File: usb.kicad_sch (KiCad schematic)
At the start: 27 parts, among them J2 USB4105, J3 USB-A-S-F-B-VU, U1 MX6UL-VM, U11 TPD4EUSB30, U12 74LVC1G04, U13 D5V0H1B2LP, U4 TUSB320, U5 AP22814AW5, U6 TPD4EUSB30, U7 D5V0H1B2LP

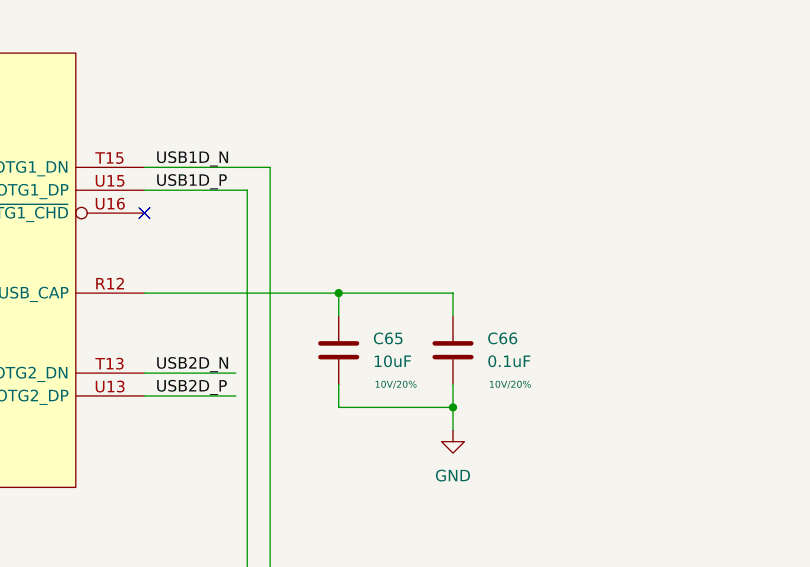
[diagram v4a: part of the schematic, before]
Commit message: lots of routing, ddr length matching done
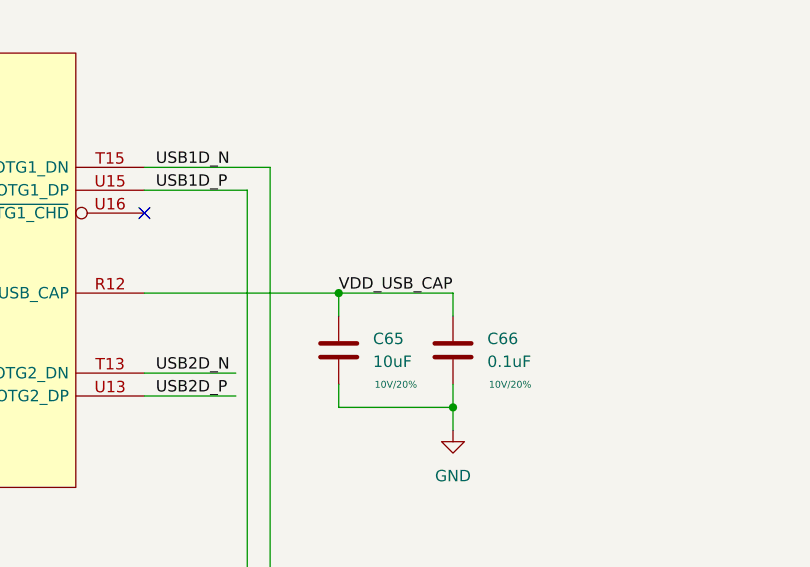
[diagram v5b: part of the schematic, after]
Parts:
- J3: footprint imx6ull-sbc:SAMTEC_USB-A-S-X-X-VU -> qsbc-zero:SAMTEC_USB-A-S-X-X-VU
- U1: footprint imx6ull-sbc:SOT1534-2 -> qsbc-zero:SOT1534-2; symbol imx6ull-sbc:MX6UL-VM -> qsbc-zero:MX6UL-VM
- U11, U6: symbol imx6ull-sbc:TPD4EUSB30 -> qsbc-zero:TPD4EUSB30
- U13, U7: footprint imx6ull-sbc:DFN100X60X45-2N -> qsbc-zero:DFN100X60X45-2N; symbol imx6ull-sbc:D5V0H1B2LP -> qsbc-zero:D5V0H1B2LP
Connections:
- net VDD_USB_CAP: now reaches C65.1, C66.1, U1.R12 (VDD_USB_CAP)
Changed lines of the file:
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@@
     (stroke (width 0) (type default) (color 0 0 0 0))
+  )
+  (label "VDD_USB_CAP" (at 130.81 80.01 0)
+    (effects (font (size 1.27 1.27)) (justify left bottom))
   )
   (label "~{USB1_INT}" (at 35.56 22.86 0)
@@
     (pin "1")
   )
-  (symbol (lib_id "imx6ull-sbc:D5V0H1B2LP") (at 298.45 60.96 270) (unit 1)
+  (symbol (lib_id "qsbc-zero:D5V0H1B2LP") (at 298.45 60.96 270) (unit 1)
     (in_bom yes) (on_board yes) (fields_autoplaced)
     (property "Reference" "U13" (id 0) (at 299.72 59.6899 90)
@@
       (effects (font (size 1.27 1.27)) (justify left))
     )
-    (property "Footprint" "imx6ull-sbc:DFN100X60X45-2N" (id 2) (at 299.72 61.087 0)
+    (property "Footprint" "qsbc-zero:DFN100X60X45-2N" (id 2) (at 299.72 61.087 0)
       (effects (font (size 1.27 1.27)) hide)
     )
@@
     (pin "1")
   )
-  (symbol (lib_id "imx6ull-sbc:MX6UL-VM") (at 76.2 53.34 0) (unit 8)
+  (symbol (lib_id "qsbc-zero:MX6UL-VM") (at 76.2 53.34 0) (unit 8)
     (in_bom yes) (on_board yes) (fields_autoplaced)
     (property "Reference" "U1" (id 0) (at 76.2 46.99 0)
@@
       (effects (font (size 1.524 1.524)))
     )
-    (property "Footprint" "imx6ull-sbc:SOT1534-2" (id 2) (at 89.154 82.804 0)
+    (property "Footprint" "qsbc-zero:SOT1534-2" (id 2) (at 89.154 82.804 0)
       (effects (font (size 1.524 1.524)) hide)
     )
@@
     (pin "1")
   )
-  (symbol (lib_id "imx6ull-sbc:TPD4EUSB30") (at 241.3 86.36 0) (unit 1)
+  (symbol (lib_id "qsbc-zero:TPD4EUSB30") (at 241.3 86.36 0) (unit 1)
     (in_bom yes) (on_board yes) (fields_autoplaced)
     (property "Reference" "U11" (id 0) (at 241.3 73.1314 0))
@@
     (pin "1")
   )
-  (symbol (lib_id "imx6ull-sbc:TPD4EUSB30") (at 135.89 207.01 0) (unit 1)
+  (symbol (lib_id "qsbc-zero:TPD4EUSB30") (at 135.89 207.01 0) (unit 1)
     (in_bom yes) (on_board yes) (fields_autoplaced)
     (property "Reference" "U6" (id 0) (at 135.89 193.7814 0))
@@
     (pin "2")
   )
-  (symbol (lib_id "imx6ull-sbc:D5V0H1B2LP") (at 181.61 208.28 0) (unit 1)
+  (symbol (lib_id "qsbc-zero:D5V0H1B2LP") (at 181.61 208.28 0) (unit 1)
     (in_bom yes) (on_board yes) (fields_autoplaced)
     (property "Reference" "U7" (id 0) (at 181.61 203.2 0))
     (property "Value" "D5V0H1B2LP" (id 1) (at 181.61 205.74 0))
-    (property "Footprint" "imx6ull-sbc:DFN100X60X45-2N" (id 2) (at 181.737 207.01 0)
+    (property "Footprint" "qsbc-zero:DFN100X60X45-2N" (id 2) (at 181.737 207.01 0)
       (effects (font (size 1.27 1.27)) hide)
     )
@@
     (property "Reference" "J3" (id 0) (at 222.25 40.64 0))
     (property "Value" "USB-A-S-F-B-VU" (id 1) (at 222.25 43.18 0))
-    (property "Footprint" "imx6ull-sbc:SAMTEC_USB-A-S-X-X-VU" (id 2) (at 226.06 54.61 0)
-      (effects (font (size 1.27 1.27)) hide)
-    )
+    (property "Footprint" "qsbc-zero:SAMTEC_USB-A-S-X-X-VU" (id 2) (at 226.06 54.61 0)
+      (effects (font (size 1.27 1.27)) hide)
+    )

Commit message: more pcb work, bom work
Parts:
- C63, C64, C69: DigiKey_PN (none) -> 490-13409-1-ND; MPN (none) -> GCM155C71A105KE38D
- C65: DigiKey_PN (none) -> 1276-1450-1-ND; MPN (none) -> CL05A106MP5NUNC
- C66: footprint Capacitor_SMD:C_0201_0603Metric -> Capacitor_SMD:C_0402_1005Metric; DigiKey_PN (none) -> 490-14603-1-ND; MPN (none) -> GRM155R71E104KE14J; Rating 10V/20% -> 25V/20%
- C67, C94: DigiKey_PN (none) -> 490-14603-1-ND; MPN (none) -> GRM155R71E104KE14J; Rating 10V/20% -> 25V/20%
- C68, C95: DigiKey_PN (none) -> 490-14603-1-ND; MPN (none) -> GRM155R71E104KE14J; Rating 6.3V/20% -> 25V/20%
- C82, C93: DigiKey_PN (none) -> 478-8198-1-ND; MPN (none) -> F931A107MBA
- J2: DigiKey_PN (none) -> 2073-USB4105-GF-ACT-ND; MPN (none) -> USB4105-GF-A
- J3: DigiKey_PN (none) -> SAM10862-ND; MPN (none) -> USB-A-S-F-B-VU
- R10, R11, R38, R39: DigiKey_PN (none) -> 311-10KJRCT-ND; MPN (none) -> RC0402JR-0710KL
- R40: DNP DNP -> (none); DigiKey_PN (none) -> 311-0.0LRCT-ND; MPN (none) -> RC0402FR-070RL
- R9: footprint Capacitor_SMD:C_0402_1005Metric -> Resistor_SMD:R_0402_1005Metric; DigiKey_PN (none) -> 311-1.0MJRCT-ND; MPN (none) -> RC0402JR-071ML
- U1: DigiKey_PN (none) -> 568-14995-ND; MPN (none) -> MCIMX6Y2DVM09AB
- U11, U6: DigiKey_PN (none) -> 296-28063-1-ND; MPN (none) -> TPD4EUSB30DQAR
- U12: DNP (none) -> DNP; DigiKey_PN (none) -> 296-26588-1-ND; MPN (none) -> SN74LVC1G04QDBVRQ1
- U13, U7: DigiKey_PN (none) -> D5V0H1B2LP-7BDICT-ND; MPN (none) -> D5V0H1B2LP-7B
- U4: DigiKey_PN (none) -> 296-43142-1-ND; MPN (none) -> TUSB320LAIRWBR
- U5: value AP22814AW5 -> AP22811B; DigiKey_PN (none) -> AP22811BW5-7DICT-ND; MPN (none) -> AP22811BW5-7
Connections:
- net USB_VBUS: now also C82.1
- net VBUS_1: no longer C82.1
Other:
- moved on the sheet: C82

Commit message: add basic readme, rev 1 of pcb
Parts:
- U12: DigiKey_PN 296-26588-1-ND -> 296-11599-1-ND; MPN SN74LVC1G04QDBVRQ1 -> SN74LVC1G04DBVR
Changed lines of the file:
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@@
       (effects (font (size 1.27 1.27)) hide)
     )
-    (property "DigiKey_PN" "296-26588-1-ND" (id 4) (at 252.73 138.43 0)
+    (property "DigiKey_PN" "296-11599-1-ND" (id 4) (at 252.73 138.43 0)
       (effects (font (size 1.27 1.27)) hide)
     )
-    (property "MPN" "SN74LVC1G04QDBVRQ1" (id 5) (at 252.73 138.43 0)
+    (property "MPN" "SN74LVC1G04DBVR" (id 5) (at 252.73 138.43 0)
       (effects (font (size 1.27 1.27)) hide)
     )

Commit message: misc rev2 fixes
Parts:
- removed C82: 100uF, Capacitor_Tantalum_SMD:CP_EIA-3528-15_AVX-H, symbol Device:C_Polarized
- added C82: 10uF, Capacitor_SMD:C_0402_1005Metric, symbol Device:C
- added C97: 0.1uF, Capacitor_SMD:C_0402_1005Metric, symbol Device:C
- C93: value 100uF -> 120uF; footprint Capacitor_Tantalum_SMD:CP_EIA-3528-15_AVX-H -> Capacitor_SMD:CP_Elec_6.3x4.9; DigiKey_PN 478-8198-1-ND -> 732-6413-1-ND; MPN F931A107MBA -> 875105244013
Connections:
- net GND: now also C82.2, C97.2
- net VBUS_1: now also C82.1, C97.1
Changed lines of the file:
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@@
   (junction (at 123.19 173.99) (diameter 0) (color 0 0 0 0)
   )
+  (junction (at 167.64 137.16) (diameter 0) (color 0 0 0 0)
+  )
   (junction (at 208.28 166.37) (diameter 0) (color 0 0 0 0)
   )
@@
   (junction (at 208.28 147.32) (diameter 0) (color 0 0 0 0)
   )
+  (junction (at 156.21 127) (diameter 0) (color 0 0 0 0)
+  )
+  (junction (at 156.21 137.16) (diameter 0) (color 0 0 0 0)
+  )
   (junction (at 142.24 147.32) (diameter 0) (color 0 0 0 0)
   )
@@
   (junction (at 115.57 161.29) (diameter 0) (color 0 0 0 0)
   )
+  (junction (at 144.78 127) (diameter 0) (color 0 0 0 0)
+  )
   (junction (at 38.1 66.04) (diameter 0) (color 0 0 0 0)
   )
@@
   )
   (junction (at 254 66.04) (diameter 0) (color 0 0 0 0)
-  )
-  (junction (at 227.33 127) (diameter 0) (color 0 0 0 0)
   )
   (no_connect (at 228.6 88.9))
@@
   (no_connect (at 106.68 189.23))
   (no_connect (at 106.68 191.77))
+  (wire (pts (xy 167.64 137.16) (xy 167.64 138.43))
+    (stroke (width 0) (type default) (color 0 0 0 0))
+  )
   (wire (pts (xy 190.5 172.72) (xy 203.2 172.72))
     (stroke (width 0) (type default) (color 0 0 0 0))
@@
     (stroke (width 0) (type default) (color 0 0 0 0))
   )
-  (wire (pts (xy 115.57 127) (xy 167.64 127))
+  (wire (pts (xy 115.57 127) (xy 144.78 127))
     (stroke (width 0) (type default) (color 0 0 0 0))
   )
@@
     (stroke (width 0) (type default) (color 0 0 0 0))
   )
+  (wire (pts (xy 156.21 127) (xy 156.21 128.27))
+    (stroke (width 0) (type default) (color 0 0 0 0))
+  )
   (wire (pts (xy 208.28 166.37) (xy 237.49 166.37))
     (stroke (width 0) (type default) (color 0 0 0 0))
@@
     (stroke (width 0) (type default) (color 0 0 0 0))
   )
-  (wire (pts (xy 167.64 135.89) (xy 167.64 138.43))
+  (wire (pts (xy 167.64 135.89) (xy 167.64 137.16))
     (stroke (width 0) (type default) (color 0 0 0 0))
   )
@@
     (stroke (width 0) (type default) (color 0 0 0 0))
   )
-  (wire (pts (xy 227.33 127) (xy 227.33 128.27))
-    (stroke (width 0) (type default) (color 0 0 0 0))
-  )
   (wire (pts (xy 209.55 132.08) (xy 209.55 138.43))
     (stroke (width 0) (type default) (color 0 0 0 0))
@@
     (stroke (width 0) (type default) (color 0 0 0 0))
   )
-  (wire (pts (xy 215.9 127) (xy 227.33 127))
-    (stroke (width 0) (type default) (color 0 0 0 0))
-  )
   (wire (pts (xy 254 60.96) (xy 254 66.04))
     (stroke (width 0) (type default) (color 0 0 0 0))
   )
+  (wire (pts (xy 144.78 127) (xy 144.78 128.27))
+    (stroke (width 0) (type default) (color 0 0 0 0))
+  )
   (wire (pts (xy 83.82 199.39) (xy 83.82 201.93))
     (stroke (width 0) (type default) (color 0 0 0 0))
@@
     (stroke (width 0) (type default) (color 0 0 0 0))
   )
+  (wire (pts (xy 156.21 135.89) (xy 156.21 137.16))
+    (stroke (width 0) (type default) (color 0 0 0 0))
+  )
   (wire (pts (xy 33.02 19.05) (xy 45.72 19.05))
     (stroke (width 0) (type default) (color 0 0 0 0))
@@
     (stroke (width 0) (type default) (color 0 0 0 0))
   )
+  (wire (pts (xy 156.21 127) (xy 167.64 127))
+    (stroke (width 0) (type default) (color 0 0 0 0))
+  )
   (wire (pts (xy 208.28 156.21) (xy 208.28 147.32))
     (stroke (width 0) (type default) (color 0 0 0 0))
@@
     (stroke (width 0) (type default) (color 0 0 0 0))
   )
+  (wire (pts (xy 156.21 137.16) (xy 167.64 137.16))
+    (stroke (width 0) (type default) (color 0 0 0 0))
+  )
   (wire (pts (xy 184.15 132.08) (xy 180.34 132.08))
     (stroke (width 0) (type default) (color 0 0 0 0))
@@
     (stroke (width 0) (type default) (color 0 0 0 0))
   )
+  (wire (pts (xy 144.78 135.89) (xy 144.78 137.16))
+    (stroke (width 0) (type default) (color 0 0 0 0))
+  )
   (wire (pts (xy 297.18 71.12) (xy 297.18 73.66))
     (stroke (width 0) (type default) (color 0 0 0 0))
@@
     (stroke (width 0) (type default) (color 0 0 0 0))
   )
-  (wire (pts (xy 227.33 127) (xy 242.57 127))
+  (wire (pts (xy 215.9 127) (xy 242.57 127))
     (stroke (width 0) (type default) (color 0 0 0 0))
   )
@@
     (stroke (width 0) (type default) (color 0 0 0 0))
   )
+  (wire (pts (xy 144.78 127) (xy 156.21 127))
+    (stroke (width 0) (type default) (color 0 0 0 0))
+  )
   (wire (pts (xy 33.02 26.67) (xy 45.72 26.67))
     (stroke (width 0) (type default) (color 0 0 0 0))
@@
     (stroke (width 0) (type default) (color 0 0 0 0))
   )
-  (wire (pts (xy 227.33 135.89) (xy 227.33 140.97))
+  (wire (pts (xy 144.78 137.16) (xy 156.21 137.16))
     (stroke (width 0) (type default) (color 0 0 0 0))
   )
@@
       (effects (font (size 1.27 1.27)) (justify left))
     )
-    (property "Value" "100uF" (id 1) (at 257.81 57.5309 0)
-      (effects (font (size 1.27 1.27)) (justify left))
-    )
-    (property "Footprint" "Capacitor_Tantalum_SMD:CP_EIA-3528-15_AVX-H" (id 2) (at 254.9652 60.96 0)
+    (property "Value" "120uF" (id 1) (at 257.81 57.5309 0)
+      (effects (font (size 1.27 1.27)) (justify left))
+    )
+    (property "Footprint" "Capacitor_SMD:CP_Elec_6.3x4.9" (id 2) (at 254.9652 60.96 0)
       (effects (font (size 1.27 1.27)) hide)
     )
@@
       (effects (font (size 0.762 0.762)))
     )
-    (property "DigiKey_PN" "478-8198-1-ND" (id 5) (at 254 57.15 0)
-      (effects (font (size 1.27 1.27)) hide)
-    )
-    (property "MPN" "F931A107MBA" (id 6) (at 254 57.15 0)
+    (property "DigiKey_PN" "732-6413-1-ND" (id 5) (at 254 57.15 0)
+      (effects (font (size 1.27 1.27)) hide)
+    )
+    (property "MPN" "875105244013" (id 6) (at 254 57.15 0)
       (effects (font (size 1.27 1.27)) hide)
     )
@@
     )
     (pin "1")
-  )
-  (symbol (lib_id "Device:C_Polarized") (at 227.33 132.08 0) (unit 1)
-    (in_bom yes) (on_board yes)
-    (property "Reference" "C82" (id 0) (at 231.14 129.9209 0)
-      (effects (font (size 1.27 1.27)) (justify left))
-    )
-    (property "Value" "100uF" (id 1) (at 231.14 132.4609 0)
-      (effects (font (size 1.27 1.27)) (justify left))
-    )
-    (property "Footprint" "Capacitor_Tantalum_SMD:CP_EIA-3528-15_AVX-H" (id 2) (at 228.2952 135.89 0)
-      (effects (font (size 1.27 1.27)) hide)
-    )
-    (property "Datasheet" "~" (id 3) (at 227.33 132.08 0)
-      (effects (font (size 1.27 1.27)) hide)
-    )
-    (property "Rating" "10V/20%" (id 4) (at 233.68 134.62 0)
-      (effects (font (size 0.762 0.762)))
-    )
-    (property "DigiKey_PN" "478-8198-1-ND" (id 5) (at 227.33 132.08 0)
-      (effects (font (size 1.27 1.27)) hide)
-    )
-    (property "MPN" "F931A107MBA" (id 6) (at 227.33 132.08 0)
-      (effects (font (size 1.27 1.27)) hide)
-    )
-    (pin "1")
-    (pin "2")
   )
   (symbol (lib_id "power:GND") (at 38.1 78.74 0) (unit 1)
@@
     (pin "2")
   )
+  (symbol (lib_id "Device:C") (at 156.21 132.08 0) (unit 1)
+    (in_bom yes) (on_board yes)
+    (property "Reference" "C97" (id 0) (at 159.385 130.8099 0)
+      (effects (font (size 1.27 1.27)) (justify left))
+    )
+    (property "Value" "0.1uF" (id 1) (at 159.385 133.3499 0)
+      (effects (font (size 1.27 1.27)) (justify left))
+    )
+    (property "Footprint" "Capacitor_SMD:C_0402_1005Metric" (id 2) (at 157.1752 135.89 0)
+      (effects (font (size 1.27 1.27)) hide)
+    )
+    (property "Datasheet" "~" (id 3) (at 156.21 132.08 0)
+      (effects (font (size 1.27 1.27)) hide)
+    )
+    (property "Rating" "25V/20%" (id 4) (at 161.29 135.255 0)
+      (effects (font (size 0.762 0.762)))
+    )
+    (property "DigiKey_PN" "490-14603-1-ND" (id 5) (at 156.21 132.08 0)
+      (effects (font (size 1.27 1.27)) hide)
+    )
+    (property "MPN" "GRM155R71E104KE14J" (id 6) (at 156.21 132.08 0)
+      (effects (font (size 1.27 1.27)) hide)
+    )
+    (pin "1")
+    (pin "2")
+  )
   (symbol (lib_id "Device:R") (at 130.81 161.29 90) (unit 1)
     (in_bom yes) (on_board yes)
@@
     )
     (property "MPN" "RC0402JR-071ML" (id 6) (at 130.81 161.29 0)
+      (effects (font (size 1.27 1.27)) hide)
+    )
+    (pin "1")
+    (pin "2")
+  )
+  (symbol (lib_id "Device:C") (at 144.78 132.08 0) (unit 1)
+    (in_bom yes) (on_board yes)
+    (property "Reference" "C82" (id 0) (at 148.59 130.8099 0)
+      (effects (font (size 1.27 1.27)) (justify left))
+    )
+    (property "Value" "10uF" (id 1) (at 148.59 133.3499 0)
+      (effects (font (size 1.27 1.27)) (justify left))
+    )
+    (property "Footprint" "Capacitor_SMD:C_0402_1005Metric" (id 2) (at 145.7452 135.89 0)
+      (effects (font (size 1.27 1.27)) hide)
+    )
+    (property "Datasheet" "~" (id 3) (at 144.78 132.08 0)
+      (effects (font (size 1.27 1.27)) hide)
+    )
+    (property "Rating" "10V/20%" (id 4) (at 151.13 135.89 0)
+      (effects (font (size 0.762 0.762)))
+    )
+    (property "DigiKey_PN" "1276-1450-1-ND" (id 5) (at 144.78 132.08 0)
+      (effects (font (size 1.27 1.27)) hide)
+    )
+    (property "MPN" "CL05A106MP5NUNC" (id 6) (at 144.78 132.08 0)
       (effects (font (size 1.27 1.27)) hide)
     )
@@
     (pin "9")
   )
-  (symbol (lib_id "power:GND") (at 227.33 140.97 0) (unit 1)
-    (in_bom yes) (on_board yes) (fields_autoplaced)
-    (property "Reference" "#PWR0153" (id 0) (at 227.33 147.32 0)
-      (effects (font (size 1.27 1.27)) hide)
-    )
-    (property "Value" "GND" (id 1) (at 227.33 145.415 0))
-    (property "Footprint" "" (id 2) (at 227.33 140.97 0)
-      (effects (font (size 1.27 1.27)) hide)
-    )
-    (property "Datasheet" "" (id 3) (at 227.33 140.97 0)
-      (effects (font (size 1.27 1.27)) hide)
-    )
-    (pin "1")
-  )
   (symbol (lib_id "Device:C") (at 266.7 57.15 0) (unit 1)
